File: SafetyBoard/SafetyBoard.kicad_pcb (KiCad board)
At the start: 4 copper layers, 154 x 93 mm, 170 parts, among them J1 Estop, J10 TSSI, J11 ACCU, J12 BBC, J13 614004135023, J14 footwell, J15 RTD B, J16 Brakelight, J17 SHOCK/WHEEL SNSR, J18 39306207, J19 AMP, J2 TS ON SW, J3 SDC OUT, J4 ACCU, J5 12v EXP, J6 PWR IN, J7 24v EXP, J8 5v EXP, J9 Current Sensor, K1 G6B-2214P-US DC12, K2 G6B-2214P-US DC12, K3 G6B-2214P-US DC12, Q1 IRLIZ44N NMOS, Q2 IRLIZ44N NMOS, Q3 IRLIZ44N NMOS, Q4 IRLIZ44N NMOS, Q5 PMOS IRF9540, Q6 PMOS IRF9540, Q7 PMOS IRF9540, SW1 SW_Push, SW2 SW_Push, SW3 SW_Push, U1 40106 Inverter, U2 4081 AND Gate, U3 LT1084-5.0, U4 LM393, U5 LM393, U6 CD4071BE OR Gate, U7 LM393, U8 LM555xN, U9 OKX-T/5-D12N-C

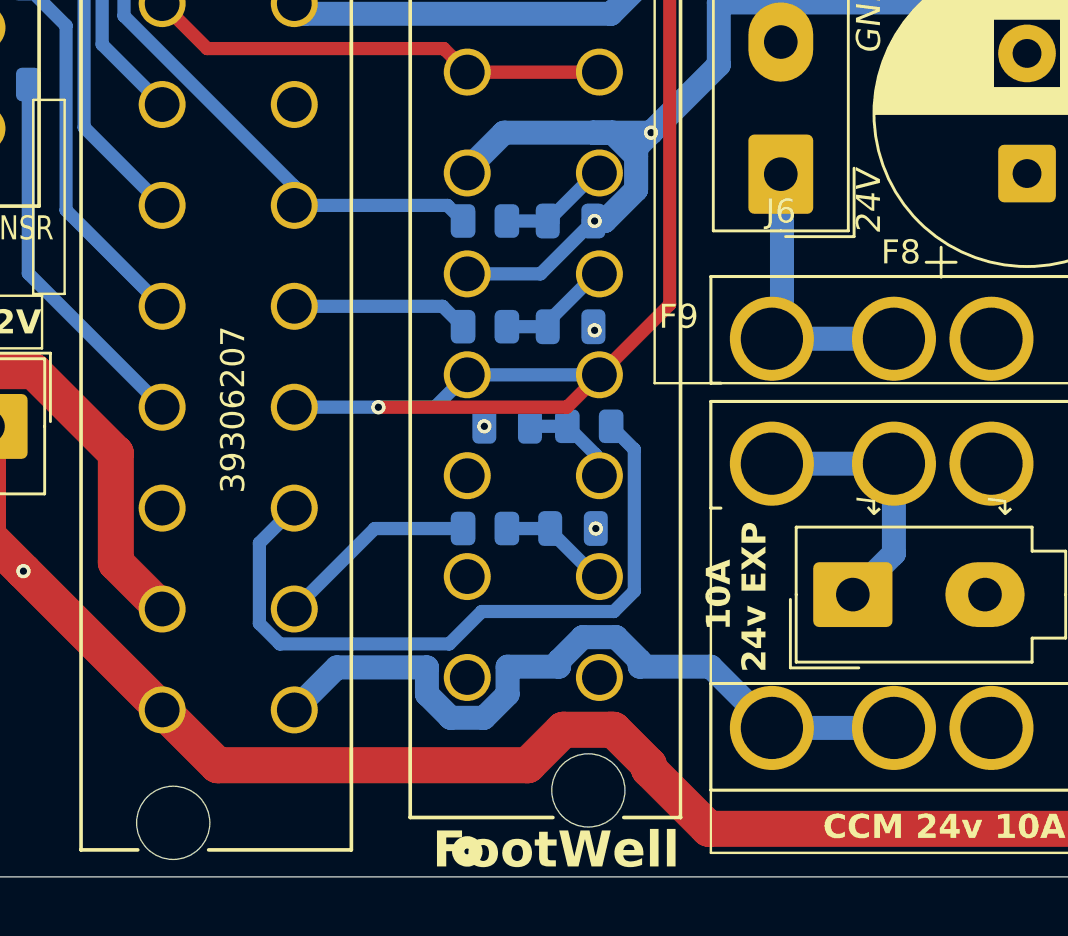
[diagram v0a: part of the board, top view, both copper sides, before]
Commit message: Connector spacing update 2
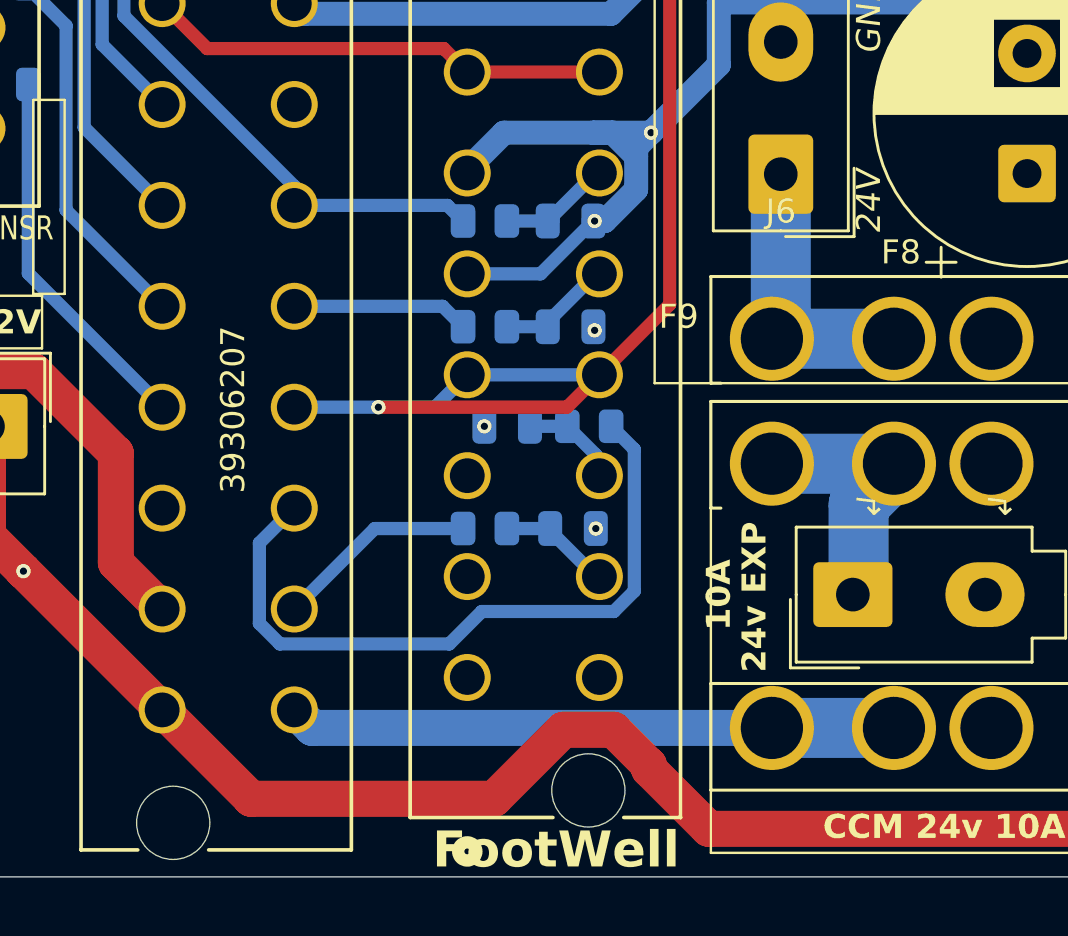
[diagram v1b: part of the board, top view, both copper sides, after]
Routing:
- net /CCM Helper/24V: track 31.1 -> 25.3 mm
- net Net-(J6-Pin_1): track 11.1 -> 12.7 mm
- net /CCM Helper/12V: track 167.5 -> 168.7 mm
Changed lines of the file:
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@@
+	)
+	(segment
+		(start 106.265003 158.354112)
+		(end 106.265003 158.515003)
+		(width 1.5)
+		(layer "F.Cu")
+		(net 73)
+	)
+	(segment
+		(start 104.785892 156.875001)
+		(end 106.265003 158.354112)
+		(width 1.5)
+		(layer "F.Cu")
+		(net 73)
 	)
 	(segment
 		(start 102.694114 156.875001)
-		(end 104.625001 156.875001)
+		(end 104.785892 156.875001)
 		(width 1.5)
+		(layer "F.Cu")
+		(net 73)
+	)
+	(segment
+		(start 99.819115 159.75)
+		(end 102.694114 156.875001)
+		(width 1.5)
+		(layer "F.Cu")
+		(net 73)
+	)
+	(segment
+		(start 89.700003 159.75)
+		(end 99.819115 159.75)
+		(width 1.5)
+		(layer "F.Cu")
+		(net 73)
+	)
+	(segment
+		(start 86 156.049997)
+		(end 89.700003 159.75)
+		(width 1.5)
+		(layer "F.Cu")
+		(net 73)
+	)
+	(segment
+		(start 170.38 159.11)
+		(end 158.133712 159.11)
+		(width 2.5)
+		(layer "F.Cu")
+		(net 73)
+	)
+	(segment
+		(start 156.243712 161)
+		(end 158.133712 159.11)
+		(width 1.5)
+		(layer "F.Cu")
+		(net 73)
+	)
+	(segment
+		(start 78.75 144.25)
+		(end 78.75 148.799998)
+		(width 1.5)
+		(layer "F.Cu")
+		(net 73)
+	)
+	(segment
+		(start 108.75 161)
+		(end 156.243712 161)
+		(width 1.5)
+		(layer "F.Cu")
+		(net 73)
+	)
+	(segment
+		(start 134.596 135.572288)
+		(end 134.596 114.869394)
+		(width 2.5)
+		(layer "F.Cu")
+		(net 73)
+	)
+	(segment
+		(start 134.596 114.869394)
+		(end 131.464106 111.7375)
+		(width 2.5)
 		(layer "F.Cu")
 		(net 73)
@@
 	)
 	(segment
-		(start 106.265003 158.354112)
-		(end 106.265003 158.515003)
-		(width 1.5)
-		(layer "F.Cu")
-		(net 73)
-	)
-	(segment
-		(start 108.75 161)
-		(end 156.243712 161)
-		(width 1.5)
-		(layer "F.Cu")
-		(net 73)
-	)
-	(segment
-		(start 170.38 159.11)
-		(end 158.133712 159.11)
-		(width 2.5)
-		(layer "F.Cu")
-		(net 73)
-	)
-	(segment
-		(start 78.75 144.25)
-		(end 78.75 148.799998)
-		(width 1.5)
-		(layer "F.Cu")
-		(net 73)
-	)
-	(segment
-		(start 134.596 135.572288)
-		(end 134.596 114.869394)
-		(width 2.5)
-		(layer "F.Cu")
-		(net 73)
-	)
-	(segment
-		(start 134.596 114.869394)
-		(end 131.464106 111.7375)
-		(width 2.5)
-		(layer "F.Cu")
-		(net 73)
-	)
-	(segment
-		(start 156.243712 161)
-		(end 158.133712 159.11)
-		(width 1.5)
-		(layer "F.Cu")
-		(net 73)
-	)
-	(segment
-		(start 86 156.049997)
-		(end 88.304115 158.354112)
-		(width 1.5)
-		(layer "F.Cu")
-		(net 73)
-	)
-	(segment
-		(start 104.625001 156.875001)
-		(end 104.785892 156.875001)
-		(width 1.5)
-		(layer "F.Cu")
-		(net 73)
-	)
-	(segment
 		(start 131.464106 111.7375)
 		(end 130.75 111.7375)
@@
 	)
 	(segment
-		(start 104.785892 156.875001)
-		(end 106.265003 158.354112)
-		(width 1.5)
-		(layer "F.Cu")
-		(net 73)
-	)
-	(segment
-		(start 101.215003 158.354112)
-		(end 102.694114 156.875001)
-		(width 1.5)
-		(layer "F.Cu")
-		(net 73)
-	)
-	(segment
 		(start 80.225001 150.274999)
 		(end 86 156.049997)
-		(width 1.5)
-		(layer "F.Cu")
-		(net 73)
-	)
-	(segment
-		(start 88.304115 158.354112)
-		(end 101.215003 158.354112)
 		(width 1.5)
 		(layer "F.Cu")
@@
 	)
 	(segment
-		(start 97.021103 154.279896)
-		(end 97.021103 155.395419)
-		(width 1)
+		(start 116.46 156.8)
+		(end 111.38 156.8)
+		(width 2.5)
 		(layer "B.Cu")
 		(net 91)
 	)
 	(segment
-		(start 93.270099 154.279897)
-		(end 97.021103 154.279896)
-		(width 1)
+		(start 91.499999 156.049997)
+		(end 92.250002 156.8)
+		(width 1.5)
 		(layer "B.Cu")
 		(net 91)
 	)
 	(segment
-		(start 91.499999 156.049997)
-		(end 93.270099 154.279897)
-		(width 1)
-		(layer "B.Cu")
-		(net 91)
-	)
-	(segment
-		(start 100.378903 155.395419)
-		(end 100.378903 154.25)
-		(width 1)
-		(layer "B.Cu")
-		(net 91)
-	)
-	(segment
-		(start 111.38 156.8)
-		(end 116.46 156.8)
-		(width 1)
-		(layer "B.Cu")
-		(net 91)
-	)
-	(segment
-		(start 100.378903 154.25)
-		(end 102.521102 154.25)
-		(width 1)
-		(layer "B.Cu")
-		(net 91)
-	)
-	(segment
-		(start 105.878902 154.25)
-		(end 108.83 154.25)
-		(width 1)
-		(layer "B.Cu")
-		(net 91)
-	)
-	(segment
-		(start 103.504578 153.021095)
-		(end 104.895426 153.021095)
-		(width 1)
-		(layer "B.Cu")
-		(net 91)
-	)
-	(segment
-		(start 98.004579 156.378895)
-		(end 99.395427 156.378895)
-		(width 1)
-		(layer "B.Cu")
-		(net 91)
-	)
-	(segment
-		(start 99.395427 156.378895)
-		(end 100.378903 155.395419)
-		(width 1)
-		(layer "B.Cu")
-		(net 91)
-	)
-	(segment
-		(start 104.895426 153.021095)
-		(end 105.878902 154.004571)
-		(width 1)
-		(layer "B.Cu")
-		(net 91)
-	)
-	(segment
-		(start 102.521102 154.25)
-		(end 102.521102 154.004571)
-		(width 1)
-		(layer "B.Cu")
-		(net 91)
-	)
-	(segment
-		(start 105.878902 154.004571)
-		(end 105.878902 154.25)
-		(width 1)
-		(layer "B.Cu")
-		(net 91)
-	)
-	(segment
-		(start 108.83 154.25)
+		(start 92.250002 156.8)
 		(end 111.38 156.8)
-		(width 1)
-		(layer "B.Cu")
-		(net 91)
-	)
-	(segment
-		(start 102.521102 154.004571)
-		(end 103.504578 153.021095)
-		(width 1)
-		(layer "B.Cu")
-		(net 91)
-	)
-	(segment
-		(start 97.021103 155.395419)
-		(end 98.004579 156.378895)
-		(width 1)
+		(width 1.5)
 		(layer "B.Cu")
 		(net 91)
@@
 	)
 	(segment
-		(start 111.38 140.6)
-		(end 116.46 140.6)
-		(width 1)
+		(start 111.75 133.75)
+		(end 111.75 140.23)
+		(width 2.5)
 		(layer "B.Cu")
 		(net 101)
 	)
 	(segment
-		(start 111.8 134.8)
-		(end 111.8 140.18)
-		(width 1)
+		(start 111.75 140.23)
+		(end 111.38 140.6)
+		(width 2.5)
+		(layer "B.Cu")
+		(net 101)
+	)
+	(segment
+		(start 116.46 140.6)
+		(end 111.38 140.6)
+		(width 2.5)
 		(layer "B.Cu")
 		(net 101)
@@
 	)
 	(segment
+		(start 116.46 146.04)
+		(end 116.46 145.8)
+		(width 2.5)
+		(layer "B.Cu")
+		(net 109)
+	)
+	(segment
+		(start 114.99 151.01)
+		(end 114.99 147.51)
+		(width 2.5)
+		(layer "B.Cu")
+		(net 109)
+	)
+	(segment
+		(start 114.75 151.25)
+		(end 114.99 151.01)
+		(width 2.5)
+		(layer "B.Cu")
+		(net 109)
+	)
+	(segment
+		(start 114.99 147.51)
+		(end 116.46 146.04)
+		(width 2.5)
+		(layer "B.Cu")
+		(net 109)
+	)
+	(segment
 		(start 116.46 145.8)
-		(end 116.46 149.54)
-		(width 1)
+		(end 111.38 145.8)
+		(width 2.5)
 		(layer "B.Cu")
 		(net 109)
-	)
-	(segment
-		(start 111.38 145.8)
-		(end 116.46 145.8)
-		(width 1)
-		(layer "B.Cu")
-		(net 109)
-	)
-	(segment
-		(start 116.46 149.54)
-		(end 114.75 151.25)
-		(width 1)
-		(layer "B.Cu")
-		(net 109)
